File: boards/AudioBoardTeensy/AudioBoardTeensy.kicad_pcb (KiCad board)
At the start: 2 copper layers, 32.2 x 51.9 mm, 11 parts, among them J1 54-00174, J3 Conn_01x20_Pin, U1 Teensy4.0

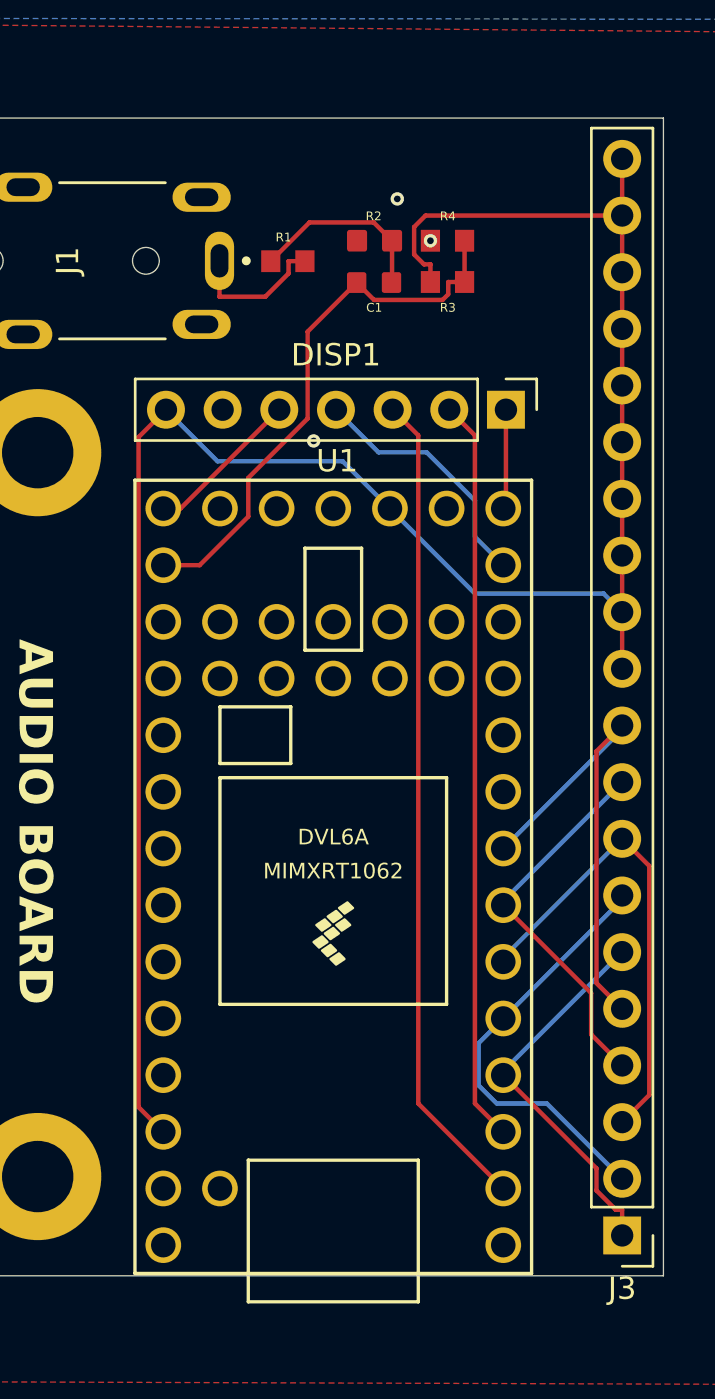
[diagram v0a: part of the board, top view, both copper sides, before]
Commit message: Final export and order audio board
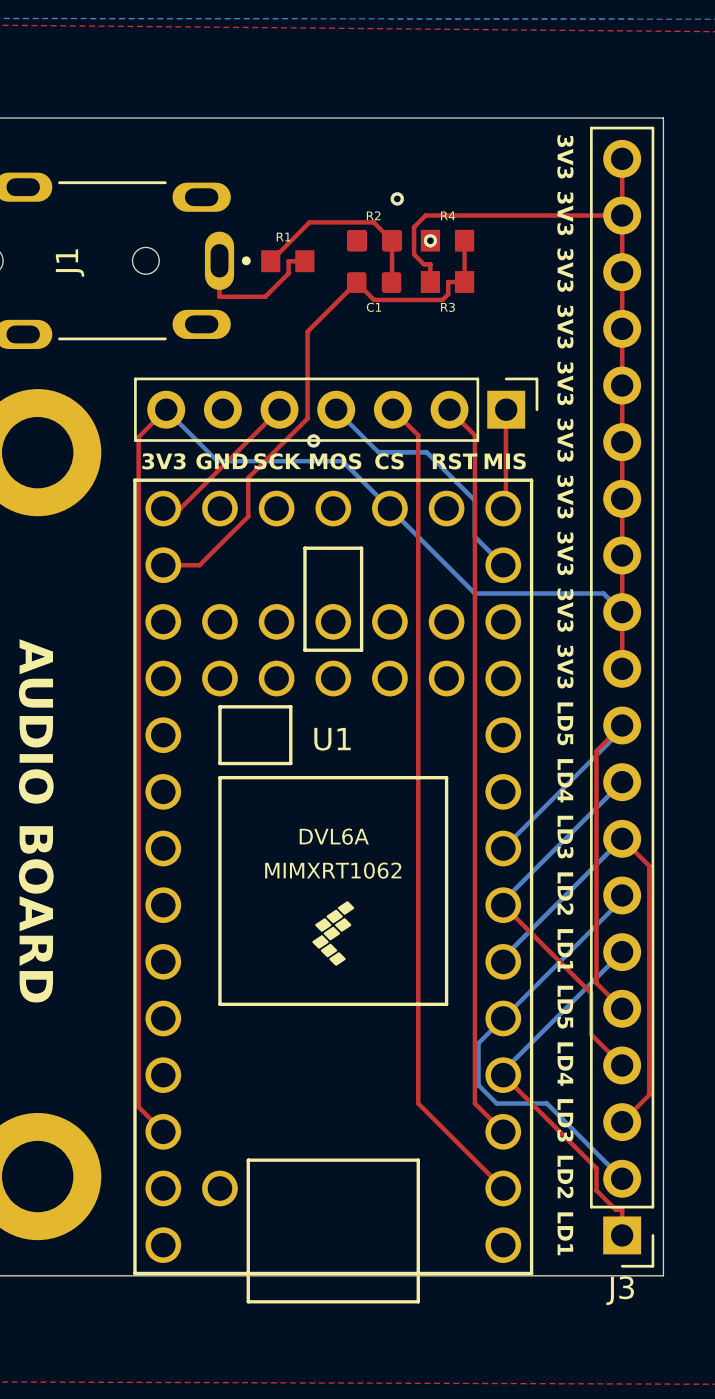
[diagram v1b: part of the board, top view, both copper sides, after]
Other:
- board text added: "3V3"
- board text added: "CS"
- board text added: "GND"
- board text added: "LD1"
- board text added: "LD2"
- board text added: "LD3"
- board text added: "LD4"
- board text added: "LD5"
- board text added: "MIS"
- board text added: "MOS"
- board text added: "RST"
- board text added: "SCK"

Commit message: Fix audio board flipped audio jack pins
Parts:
- moved R1 2.90 mm to (142.6, 75.5), turned to 180 degrees
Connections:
- J1 pad 1: AUDIO -> GND
- J1 pad 2: GND -> AUDIO
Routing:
- net AUDIO: track 6.42 -> 2.92 mm
- net Net-(C1-Pad2): track 8.38 -> 7.31 mm
- net GND: vias 3 -> 10
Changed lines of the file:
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@@
 			)
 		)
+		(property "LCSC" "C2907088"
+			(at 0 0 0)
+			(unlocked yes)
+			(layer "F.Fab")
+			(hide yes)
+			(effects
+				(font
+					(size 1 1)
+					(thickness 0.15)
+				)
+			)
+		)
 		(property ki_fp_filters "R_*")
 		(sheetname "/")
@@
 		(sheetname "/")
 		(sheetfile "AudioBoardTeensy.kicad_sch")
-		(attr through_hole exclude_from_pos_files exclude_from_bom)
+		(attr through_hole exclude_from_pos_files)
 		(fp_line
 			(start -3.5 5.5)
@@
 			(layers "*.Cu" "*.Mask")
 			(remove_unused_layers no)
-			(net 14 "AUDIO")
+			(net 3 "GND")
 			(pintype "passive")
 			(solder_mask_margin 0.102)
@@
 			(layers "*.Cu" "*.Mask")
 			(remove_unused_layers no)
-			(net 3 "GND")
+			(net 14 "AUDIO")
 			(pintype "passive")
 			(solder_mask_margin 0.102)
@@
 		(sheetname "/")
 		(sheetfile "AudioBoardTeensy.kicad_sch")
-		(attr through_hole exclude_from_pos_files exclude_from_bom)
+		(attr through_hole exclude_from_pos_files)
 		(fp_line
 			(start 17.78 -8.89)
@@
 		(sheetname "/")
 		(sheetfile "AudioBoardTeensy.kicad_sch")
-		(attr through_hole exclude_from_pos_files exclude_from_bom)
+		(attr through_hole exclude_from_pos_files)
 		(fp_line
 			(start -1.38 16.62)
@@
 	(footprint "Resistor1K:RCG06031K00FKEA"
 		(layer "F.Cu")
-		(at 142.7425 78.3922)
+		(at 142.55 75.5 180)
 		(property "Reference" "R1"
-			(at -0.19 -1.07 0)
+			(at -0.0075 -1.1578 0)
 			(layer "F.SilkS")
 			(effects
@@
 		(attr smd)
 		(fp_line
-			(start -1.444 -0.74)
+			(start 1.444 0.74)
 			(end 1.444 -0.74)
 			(stroke
@@
 		(fp_line
 			(start -1.444 0.74)
-			(end -1.444 -0.74)
+			(end 1.444 0.74)
 			(stroke
 				(width 0.05)
@@
 		(fp_line
 			(start -1.444 0.74)
-			(end 1.444 0.74)
+			(end -1.444 -0.74)
 			(stroke
 				(width 0.05)
@@
 		)
 		(fp_line
-			(start 1.444 0.74)
+			(start -1.444 -0.74)
 			(end 1.444 -0.74)
 			(stroke
@@
 		)
 		(fp_line
-			(start -0.83 0.47)
-			(end -0.83 -0.47)
+			(start 0.83 0.47)
+			(end 0.83 -0.47)
 			(stroke
 				(width 0.127)
@@
 		)
 		(fp_line
-			(start 0.83 -0.47)
-			(end -0.83 -0.47)
+			(start 0.83 0.47)
+			(end -0.83 0.47)
 			(stroke
 				(width 0.127)
@@
 		)
 		(fp_line
-			(start 0.83 0.47)
-			(end -0.83 0.47)
+			(start 0.83 -0.47)
+			(end -0.83 -0.47)
 			(stroke
 				(width 0.127)
@@
 		)
 		(fp_line
-			(start 0.83 0.47)
-			(end 0.83 -0.47)
+			(start -0.83 0.47)
+			(end -0.83 -0.47)
 			(stroke
 				(width 0.127)
@@
 		)
 		(pad "1" smd rect
-			(at -0.765 0)
+			(at -0.765 0 180)
 			(size 0.86 0.98)
 			(layers "F.Cu" "F.Mask" "F.Paste")
@@
 		)
 		(pad "2" smd rect
-			(at 0.765 0)
+			(at 0.765 0 180)
 			(size 0.86 0.98)
 			(layers "F.Cu" "F.Mask" "F.Paste")
@@
 		(sheetname "/")
 		(sheetfile "AudioBoardTeensy.kicad_sch")
-		(attr through_hole exclude_from_pos_files exclude_from_bom)
+		(attr through_hole exclude_from_pos_files)
 		(fp_line
 			(start 1.38 1.27)
@@
 	)
 	(segment
-		(start 146.5932 76.6532)
-		(end 143.7165 76.6532)
+		(start 147.415 76.615)
+		(end 147.415 77.475)
 		(width 0.2)
 		(layer "F.Cu")
@@
 	)
 	(segment
-		(start 147.415 77.475)
-		(end 146.5932 76.6532)
+		(start 143.315 75.5)
+		(end 146.3 75.5)
 		(width 0.2)
 		(layer "F.Cu")
@@
 	)
 	(segment
-		(start 143.7165 76.6532)
-		(end 141.9775 78.3922)
+		(start 146.3 75.5)
+		(end 147.415 76.615)
 		(width 0.2)
 		(layer "F.Cu")
@@
 	)
 	(via
+		(at 140.6 92.3)
+		(size 0.6)
+		(drill 0.3)
+		(layers "F.Cu" "B.Cu")
+		(free yes)
+		(net 3)
+	)
+	(via
 		(at 143.9 86.45)
 		(size 0.6)
@@
 	)
 	(via
+		(at 139.4 117.65)
+		(size 0.6)
+		(drill 0.3)
+		(layers "F.Cu" "B.Cu")
+		(free yes)
+		(net 3)
+	)
+	(via
 		(at 149.135 77.475)
 		(size 0.6)
@@
 		(net 3)
 	)
+	(via
+		(at 150.25 122.7)
+		(size 0.6)
+		(drill 0.3)
+		(layers "F.Cu" "B.Cu")
+		(free yes)
+		(net 3)
+	)
+	(via
+		(at 154.2 118.45)
+		(size 0.6)
+		(drill 0.3)
+		(layers "F.Cu" "B.Cu")
+		(free yes)
+		(net 3)
+	)
+	(via
+		(at 147.15 99.6)
+		(size 0.6)
+		(drill 0.3)
+		(layers "F.Cu" "B.Cu")
+		(free yes)
+		(net 3)
+	)
+	(via
+		(at 144.15 77.5)
+		(size 0.6)
+		(drill 0.3)
+		(layers "F.Cu" "B.Cu")
+		(free yes)
+		(net 3)
+	)
+	(via
+		(at 147.4 92.05)
+		(size 0.6)
+		(drill 0.3)
+		(layers "F.Cu" "B.Cu")
+		(free yes)
+		(net 3)
+	)
 	(segment
 		(start 142.36 85.05)
@@
 	)
 	(segment
-		(start 141.7321 79.9847)
-		(end 142.7758 78.941)
-		(width 0.2)
-		(layer "F.Cu")
-		(net 14)
-	)
-	(segment
-		(start 142.7758 78.941)
-		(end 142.7758 78.3922)
-		(width 0.2)
-		(layer "F.Cu")
-		(net 14)
-	)
-	(segment
-		(start 139.68 79.9847)
-		(end 141.7321 79.9847)
-		(width 0.2)
-		(layer "F.Cu")
-		(net 14)
-	)
-	(segment
-		(start 139.68 78.375)
-		(end 139.68 79.9847)
+		(start 141.76 75.525)
+		(end 141.785 75.5)
 		(width 0.2)
 		(layer "F.Cu")
@@
 	)
 	(segment
-		(start 143.5075 78.3922)
-		(end 142.7758 78.3922)
+		(start 138.88 75.525)
+		(end 141.76 75.525)
 		(width 0.2)
 		(layer "F.Cu")

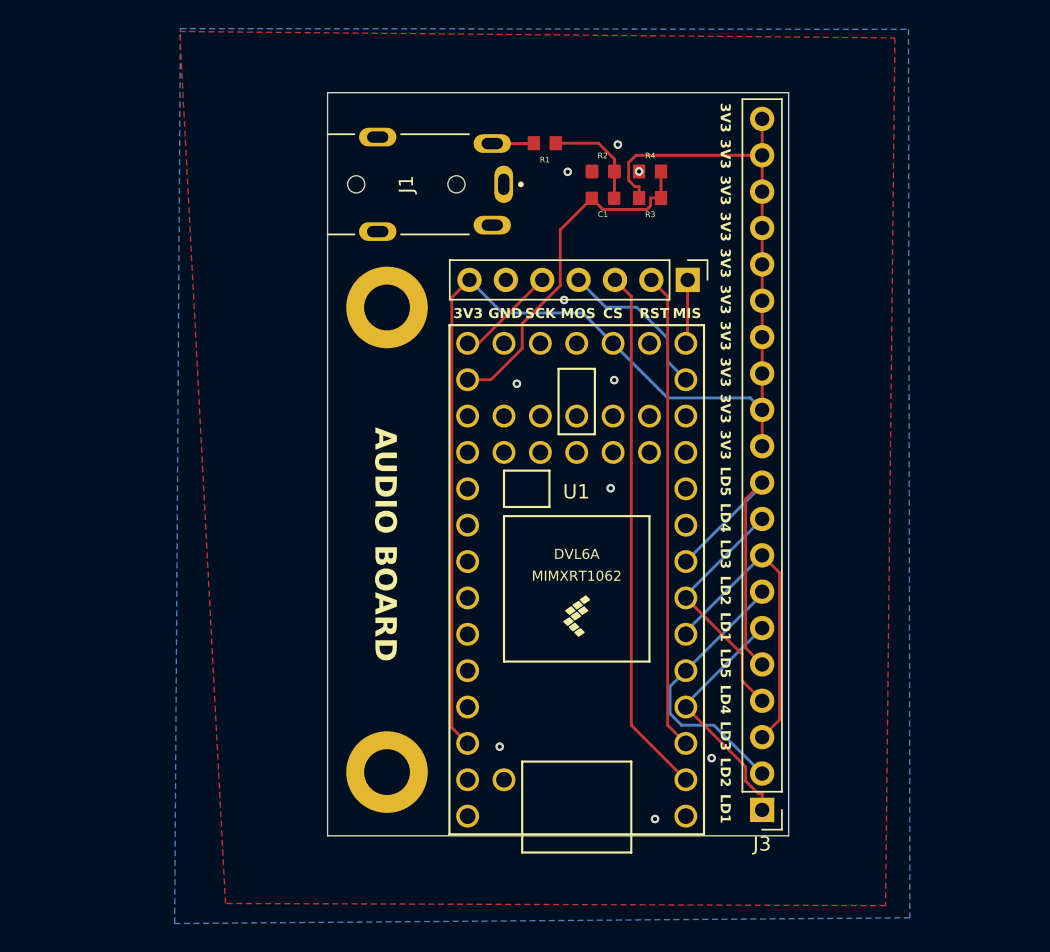
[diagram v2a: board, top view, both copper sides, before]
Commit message: Re-route audio board
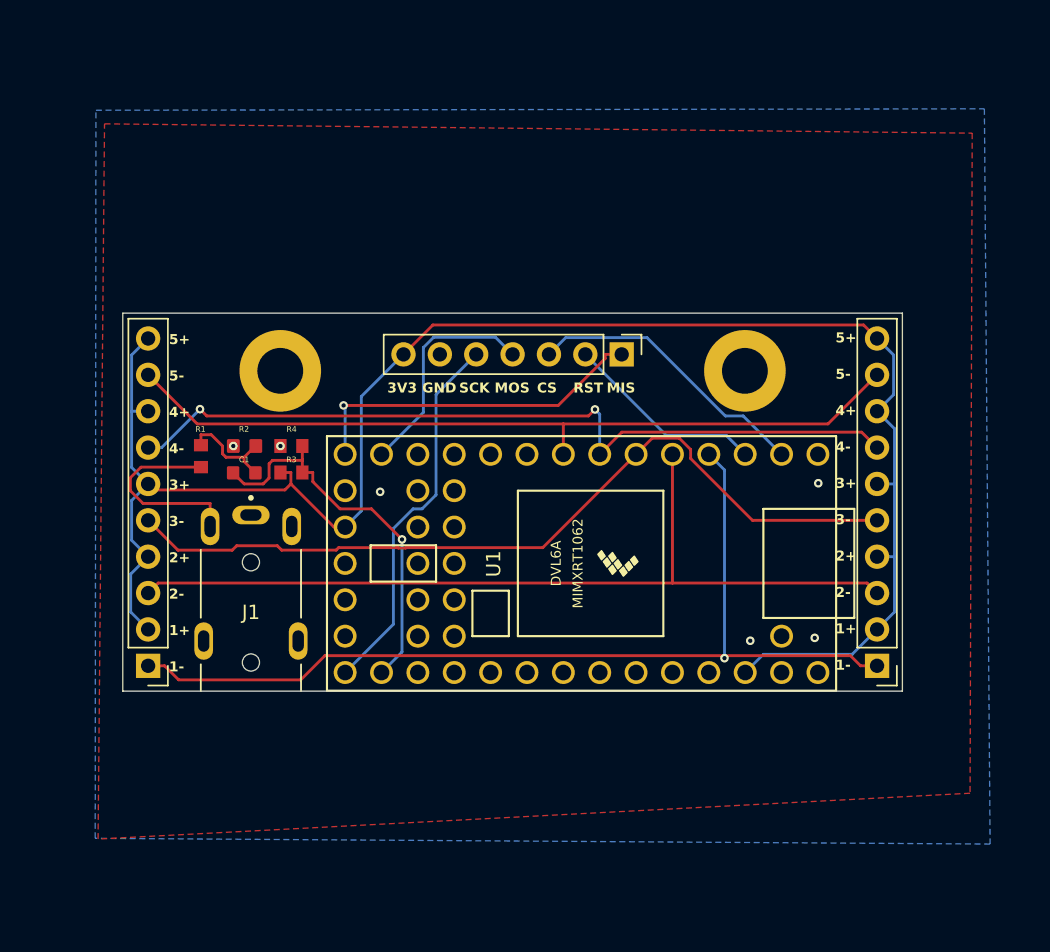
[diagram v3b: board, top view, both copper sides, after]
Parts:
- added J2: Conn_01x10_Pin, Connector_PinHeader_2.54mm:PinHeader_1x10_P2.54mm_Vertical, F.Cu at (114.8, 112.0)
- J3: value Conn_01x20_Pin -> Conn_01x10_Pin; footprint Connector_PinHeader_2.54mm:PinHeader_1x20_P2.54mm_Vertical -> Connector_PinHeader_2.54mm:PinHeader_1x10_P2.54mm_Vertical
- moved H2 37.6 mm to (156.5, 91.4), turned to 90 degrees
- moved R1 32.5 mm to (118.5, 97.4), turned to -90 degrees
- moved J1 31.8 mm to (122.0, 108.3), turned to 0 degrees
- moved C1 31.5 mm to (121.6, 98.5)
- moved R4 31.5 mm to (124.8, 96.7)
- moved R2 31.5 mm to (121.6, 96.7)
- moved R3 31.5 mm to (124.8, 98.5)
- moved J3 12.9 mm to (165.8, 112.0)
- moved H1 8.67 mm to (124.1, 91.4), turned to 90 degrees
- moved DISP1 6.95 mm to (147.9, 90.2)
- moved U1 1.19 mm to (145.1, 104.8), turned to 180 degrees
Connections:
- J3 pad 10: LED5 -> +3V3
- J3 pad 2: LED2 -> +3V3
- J3 pad 3: LED3 -> LED2
- J3 pad 4: LED4 -> +3V3
- J3 pad 5: LED5 -> LED3
- J3 pad 6: LED1 -> +3V3
- J3 pad 7: LED2 -> LED4
- J3 pad 8: LED3 -> +3V3
- J3 pad 9: LED4 -> LED5
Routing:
- net LED1: track 17.3 -> 67.2 mm, vias 0 -> 1
- net LED2: track 19.3 -> 60.5 mm
- net LED4: track 17.1 -> 56.4 mm, vias 0 -> 2
- net LED3: track 21.4 -> 58.0 mm
- net LED5: track 21.4 -> 55.9 mm
- net +3V3: track 92.9 -> 124.5 mm
- net MISO: track 4.48 -> 24.5 mm, vias 0 -> 1
- net SCK: track 7.03 -> 26.4 mm
- net RST: track 33.4 -> 14.1 mm
- net CS: track 37.0 -> 20.1 mm
- net AUDIO: track 2.92 -> 13.7 mm
- net MOSI: track 11.3 -> 15.7 mm
- net A0: track 24.9 -> 27.4 mm, vias 0 -> 1
- net GND: vias 10 -> 6
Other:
- board size 32.2 x 51.9 mm -> 54.5 x 26.4 mm
- board text added: "1+"
- board text added: "1-"
- board text added: "2+"
- board text added: "2-"
- board text added: "3+"
- board text added: "3-"
- board text added: "4+"
- board text added: "4-"
- board text added: "5+"
- board text added: "5-"
- board text removed: "AUDIO BOARD"
- board text removed: "LD1"
- board text removed: "LD2"
- board text removed: "LD3"
- board text removed: "LD4"
- board text removed: "LD5"

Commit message: Another iteration of boards
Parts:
- removed DISP1: DFR0934, Connector_PinHeader_2.54mm:PinHeader_1x07_P2.54mm_Vertical
- added J4: DFR0934, Connector_PinHeader_2.54mm:PinHeader_1x07_P2.54mm_Vertical, F.Cu at (147.9, 90.2)
- moved R1 0.62 mm to (119.2, 97.3)
- moved C1 0.30 mm to (121.6, 98.8)
- moved R3 0.30 mm to (124.8, 98.8)
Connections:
- J1 pad 2: AUDIO -> GND
- J1 pad 3: unconnected-(J1-Pad3) -> /RING 1
- J1 pad 4_1: unconnected-(J1-Pad4_1) -> AUDIO
- J1 pad 4_2: unconnected-(J1-Pad4_2) -> /TIP 2
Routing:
- net +3V3: track 124.5 -> 140.7 mm, vias 0 -> 2
- net LED2: track 60.5 -> 71.0 mm
- net A0: track 27.4 -> 34.9 mm
- net LED1: track 67.2 -> 72.6 mm, vias 1 -> 0
- net GND: track 0.00 -> 2.73 mm, vias 6 -> 2
- net LED3: track 58.0 -> 55.7 mm
- net LED4: track 56.4 -> 54.7 mm, vias 2 -> 0
- net Net-(C1-Pad2): track 7.28 -> 6.18 mm
- net AUDIO: track 13.7 -> 14.5 mm, vias 0 -> 1
- removed copper zone on F.Cu, net GND

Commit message: Re-finalize audio board and cleanup
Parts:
- moved J4 3.28 mm to (150.5, 92.2)
- moved J1 0.53 mm to (122.0, 108.8)
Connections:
- J1 pad 2: GND -> AUDIO
- J1 pad 3: /RING 1 -> GND
- J1 pad 4_1: AUDIO -> /TIP 1
- J2 pad 2: +3V3 -> LED2
- J2 pad 3: LED2 -> LED3
- J2 pad 4: +3V3 -> LED4
- J2 pad 5: LED3 -> LED5
- J2 pad 7: LED4 -> +3V3
- J2 pad 9: LED5 -> +3V3
- J3 pad 2: +3V3 -> LED2
- J3 pad 3: LED2 -> LED3
- J3 pad 4: +3V3 -> LED4
- J3 pad 5: LED3 -> LED5
- J3 pad 7: LED4 -> +3V3
- J3 pad 9: LED5 -> +3V3
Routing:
- net +3V3: track 140.7 -> 114.7 mm, vias 2 -> 3
- net AUDIO: track 14.5 -> 4.71 mm, vias 1 -> 0
- net LED1: track 72.6 -> 80.3 mm
- net A0: track 34.9 -> 28.3 mm
- net LED2: track 71.0 -> 65.4 mm, vias 0 -> 1
- net LED3: track 55.7 -> 61.3 mm, vias 0 -> 1
- net LED4: track 54.7 -> 58.6 mm, vias 0 -> 1
- net GND: track 2.73 -> 6.50 mm, vias 2 -> 7
- net RST: track 14.1 -> 10.7 mm
- net CS: track 20.5 -> 17.1 mm
- net LED5: track 55.9 -> 58.2 mm
- net MOSI: track 15.7 -> 13.8 mm
- net MISO: track 24.3 -> 25.5 mm, vias 1 -> 0
- net SCK: track 26.4 -> 27.5 mm
- added copper zone on F.Cu, net GND
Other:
- board size 54.5 x 26.4 mm -> 54.5 x 33 mm
- board text added: "+"
- board text removed: "1+"
- board text removed: "2+"
- board text removed: "3+"
- board text removed: "4+"
- board text removed: "5+"
